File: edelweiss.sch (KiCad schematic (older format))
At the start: 20 parts, among them J1 NEIGHBOR1, J2 NEIGHBOR2, J7 BONUS_ROW

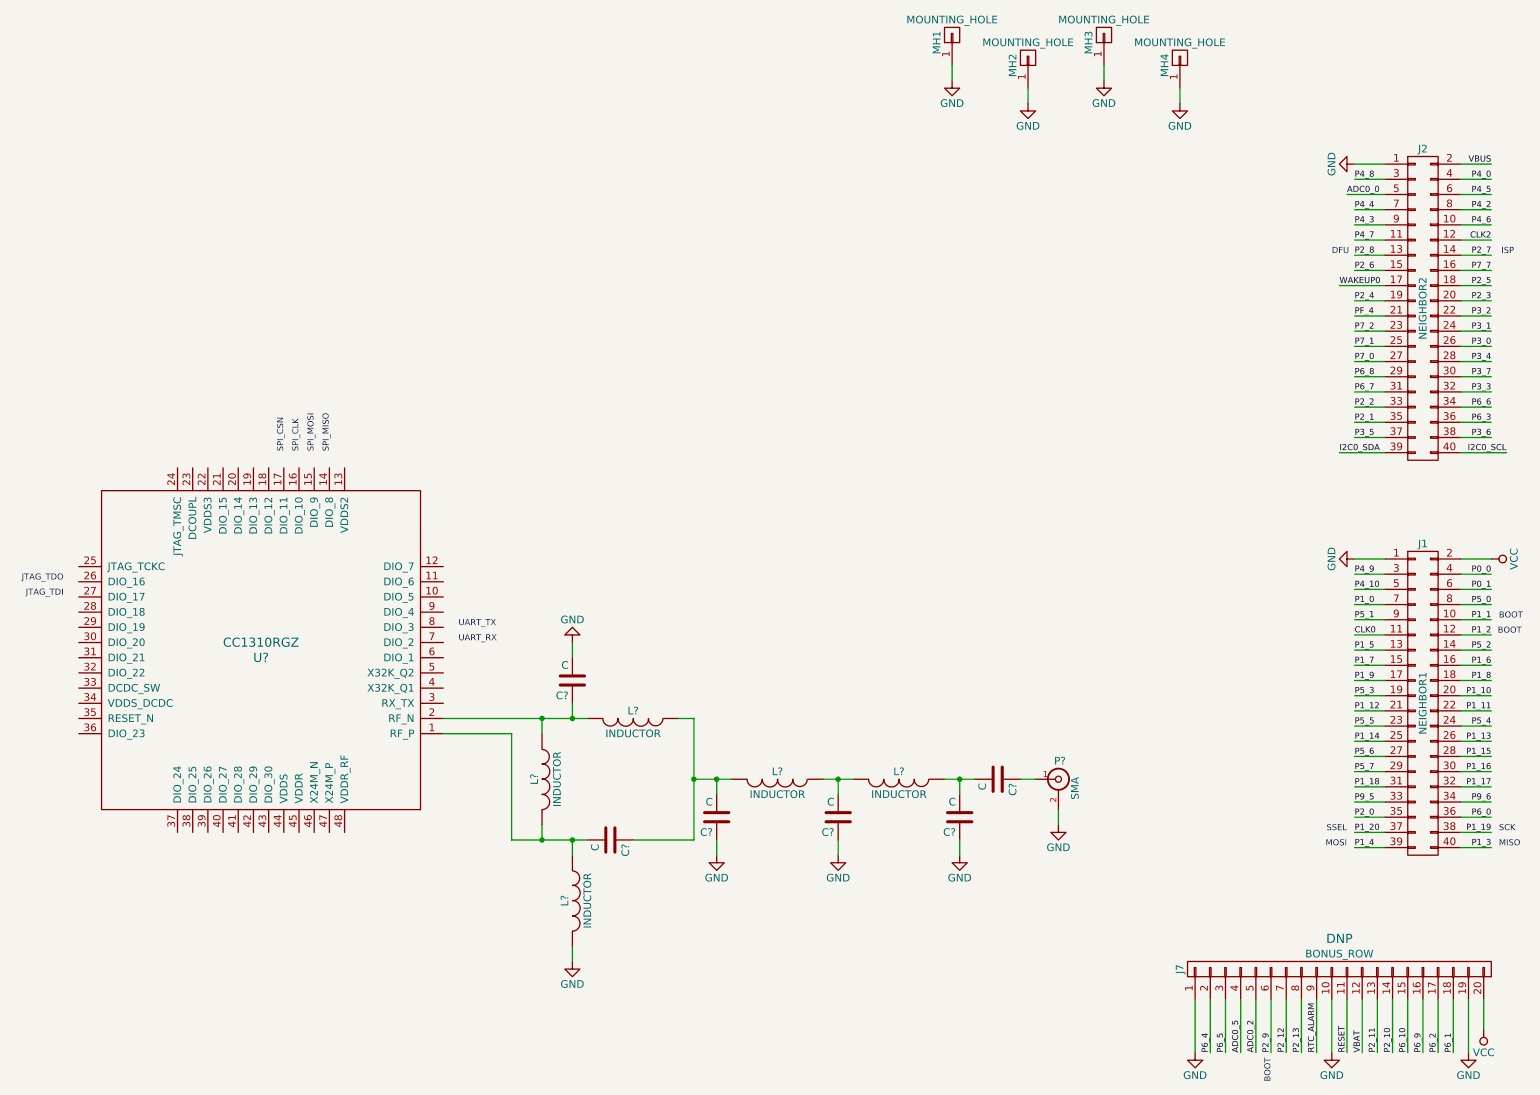
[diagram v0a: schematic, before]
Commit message: adopt OSHWA convention for SPI signal names https://www.oshwa.org/a-resolution-to-redefine-spi-signal-names
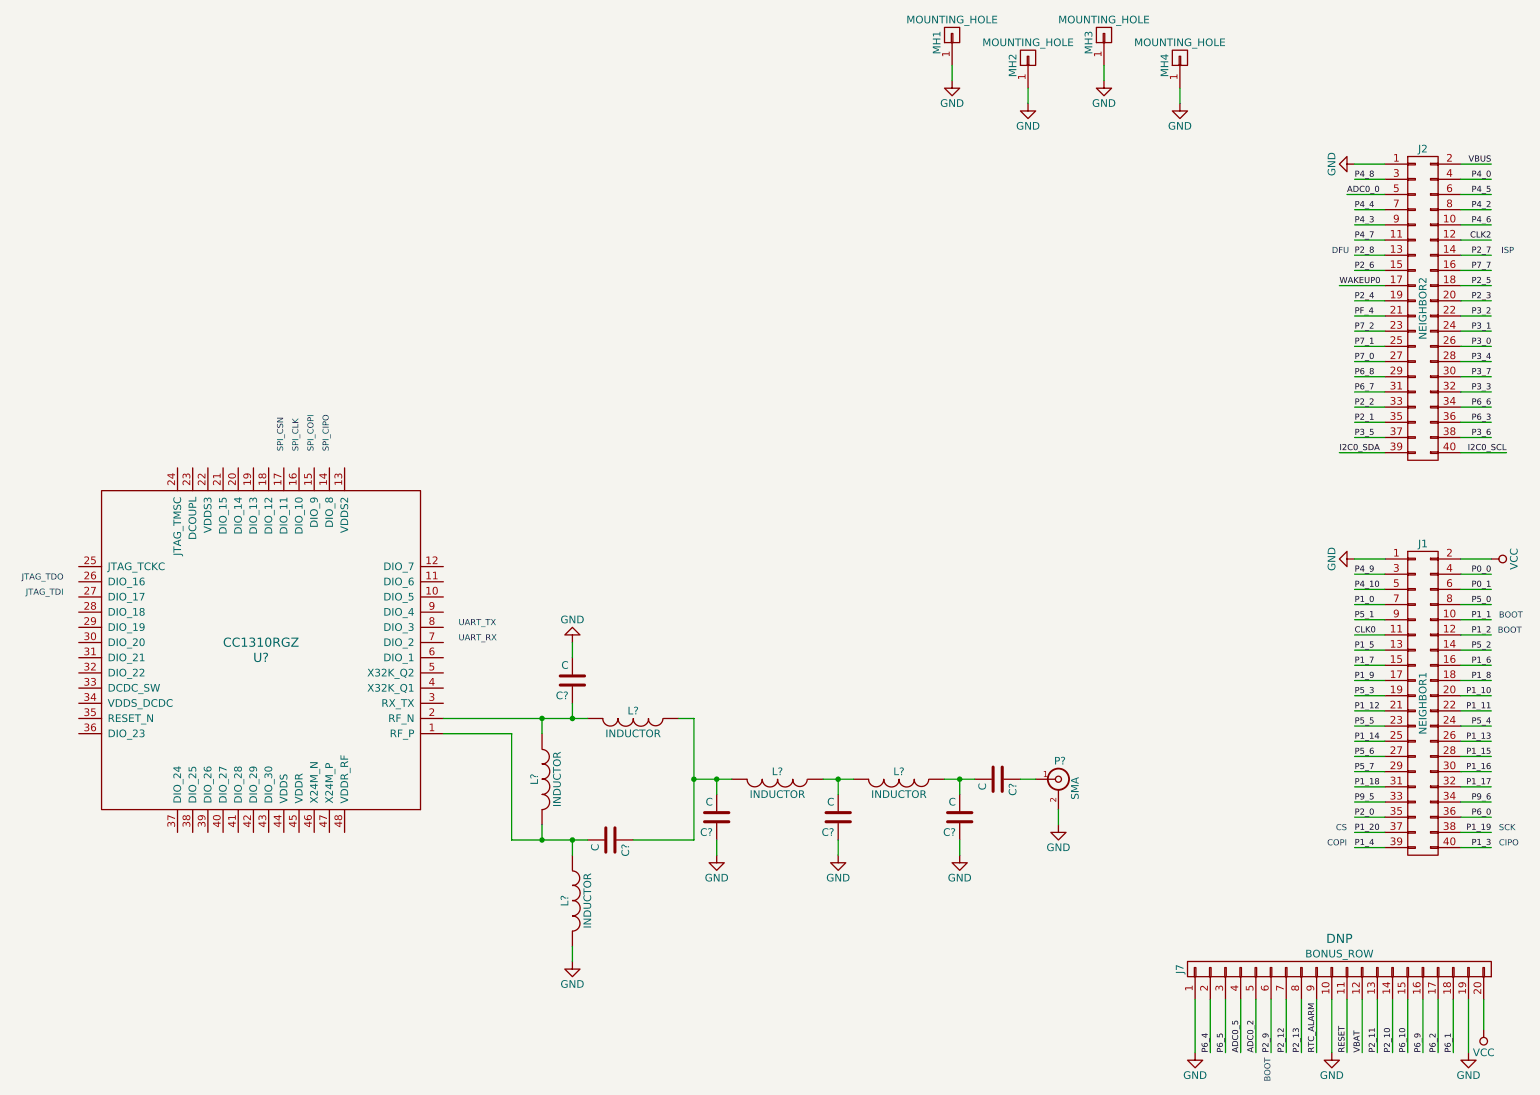
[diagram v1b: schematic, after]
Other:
- note added: "CIPO"
- note added: "COPI"
- note added: "CS"
- note added: "SPI_CIPO"
- note added: "SPI_COPI"
- note removed: "MISO"
- note removed: "MOSI"
- note removed: "SPI_MISO"
- note removed: "SPI_MOSI"
- note removed: "SSEL"
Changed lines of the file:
@@
 P2_0
 Text Notes 16250 6200 0    40   ~ 0
-MISO
+CIPO
 Text Notes 15250 6200 2    40   ~ 0
-MOSI
+COPI
 Text Notes 16250 6100 0    40   ~ 0
 SCK
 Text Notes 15250 6100 2    40   ~ 0
-SSEL
+CS
 Text Label 16300 3600 2    40   ~ 0
 I2C0_SCL
@@
 SPI_CSN
 Text Notes 8450 3600 1    40   ~ 0
-SPI_MOSI
+SPI_COPI
 Text Notes 8550 3600 1    40   ~ 0
-SPI_MISO
+SPI_CIPO
 Text Notes 6800 4450 2    40   ~ 0
 JTAG_TDO
